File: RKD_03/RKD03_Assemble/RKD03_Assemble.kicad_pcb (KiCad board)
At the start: 2 copper layers, 97.7 x 97.6 mm, 36 parts, among them SW1 SW_Push, SW10 SW_Push, SW11 RotaryEncoder_Switch, SW12 SW_Push, SW13 SW_Push, SW14 RotaryEncoder_Switch, SW2 RotaryEncoder_Switch, SW3 SW_Push, SW4 SW_Push, SW5 RotaryEncoder_Switch, SW6 SW_Push, SW7 SW_Push, SW8 RotaryEncoder_Switch, SW9 SW_Push, U1 Pico

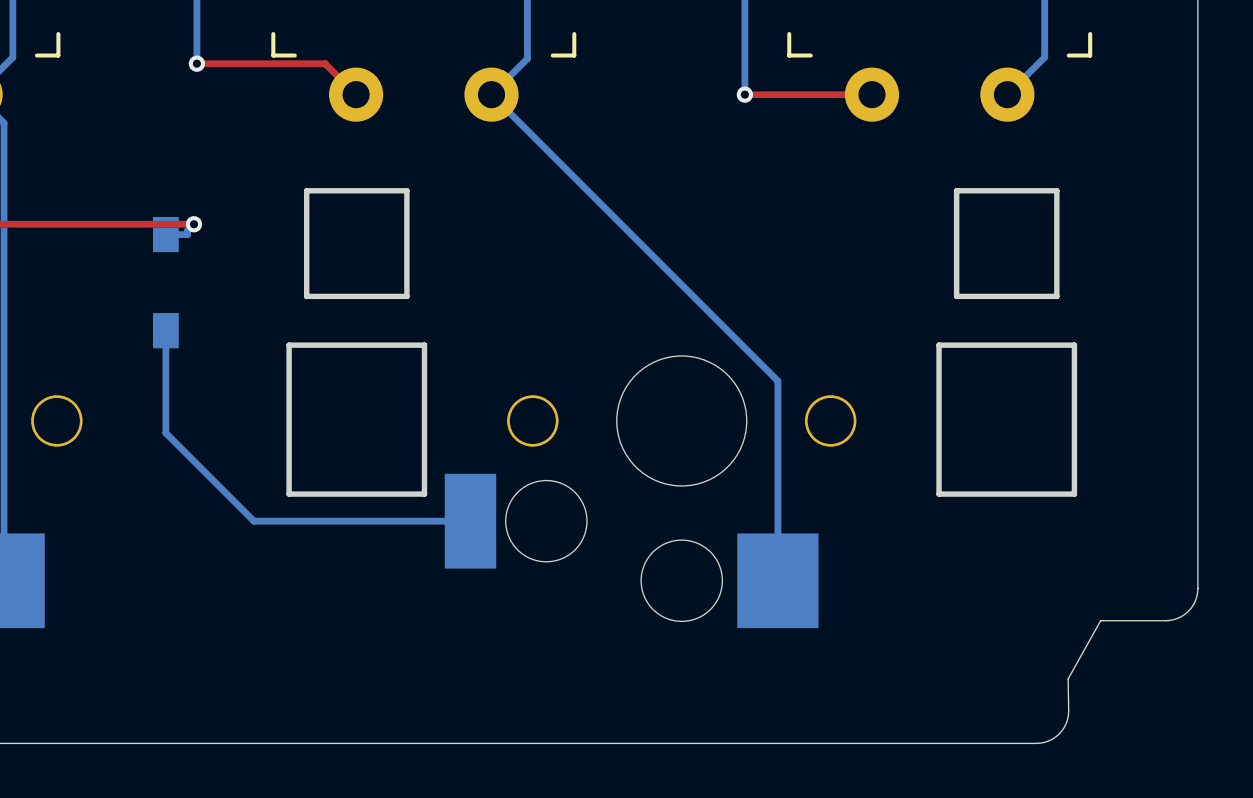
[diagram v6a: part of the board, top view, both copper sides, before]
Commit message: RKD03 新フットプリントの検証
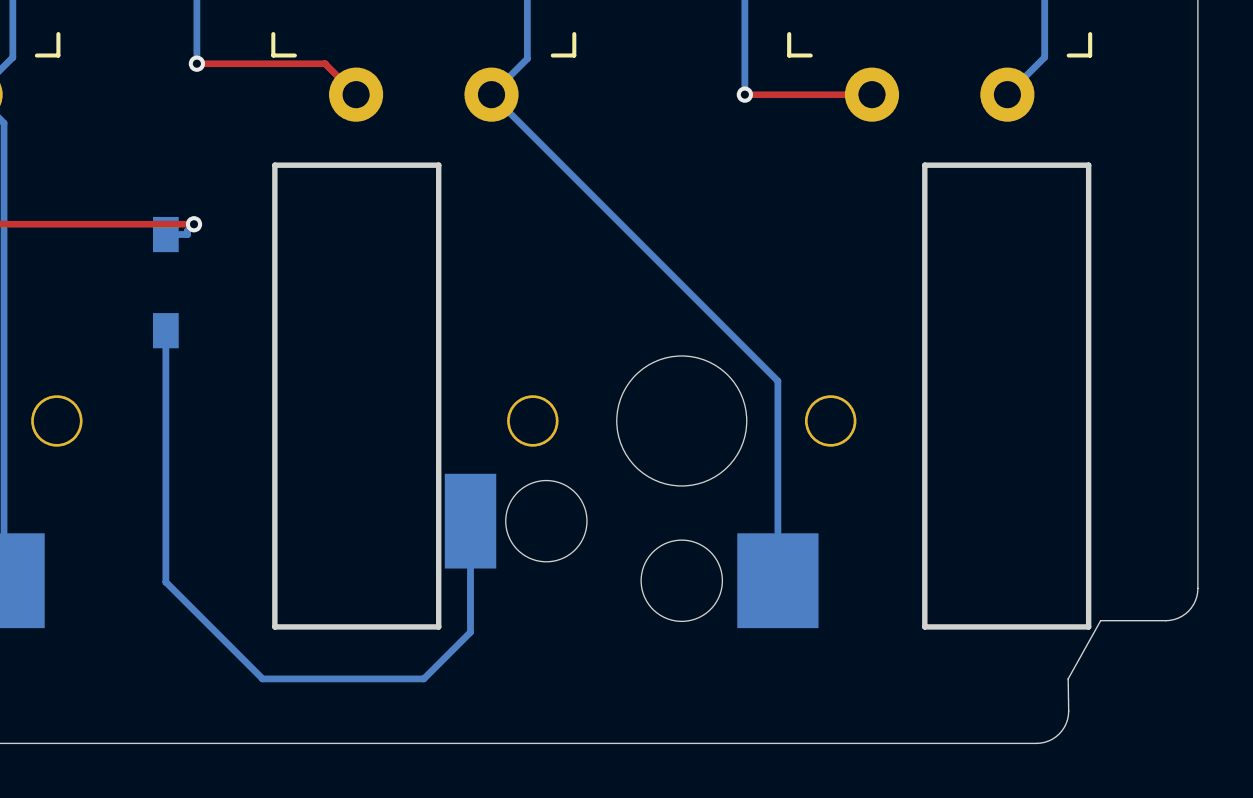
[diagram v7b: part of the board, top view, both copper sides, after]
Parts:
- SW12: footprint Rikkodo_FootPrint:rkd_Choc_v1v2_Hotswap_2u -> Rikkodo_FootPrint:rkd_Choc_v1v2_Hotswap_2u_Gat
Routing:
- net Net-(D12-A): track 16.4 -> 26.8 mm
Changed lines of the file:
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@@
 		)
 	)
-	(footprint "Rikkodo_FootPrint:rkd_Choc_v1v2_Hotswap_2u"
+	(footprint "Rikkodo_FootPrint:rkd_Choc_v1v2_Hotswap_2u_Gat"
 		(layer "F.Cu")
 		(at 121.44375 102.39375)
@@
 			)
 		)
-		(property "Footprint" "Rikkodo_FootPrint:rkd_Choc_v1v2_Hotswap_2u"
+		(property "Footprint" "Rikkodo_FootPrint:rkd_Choc_v1v2_Hotswap_2u_Gat"
 			(at 0 0 0)
 			(layer "F.Fab")
@@
 		)
 		(fp_line
-			(start -14.5 -2.8)
-			(end -9.5 -2.8)
+			(start -15.025 -9.445)
+			(end -8.975 -9.445)
 			(stroke
 				(width 0.2)
@@
 		)
 		(fp_line
-			(start -14.5 2.7)
-			(end -14.5 -2.8)
+			(start -15.025 7.605)
+			(end -15.025 -9.445)
 			(stroke
 				(width 0.2)
@@
 		)
 		(fp_line
-			(start -13.85 -8.5)
-			(end -10.15 -8.5)
+			(start -8.975 -9.445)
+			(end -8.975 7.605)
 			(stroke
 				(width 0.2)
@@
 		)
 		(fp_line
-			(start -13.85 -4.6)
-			(end -13.85 -8.5)
+			(start -8.975 7.605)
+			(end -15.025 7.605)
 			(stroke
 				(width 0.2)
@@
 		)
 		(fp_line
-			(start -10.15 -8.5)
-			(end -10.15 -4.6)
+			(start 8.975 -9.445)
+			(end 8.975 7.605)
 			(stroke
 				(width 0.2)
@@
 		)
 		(fp_line
-			(start -10.15 -4.6)
-			(end -13.85 -4.6)
+			(start 8.975 7.605)
+			(end 15.025 7.605)
 			(stroke
 				(width 0.2)
@@
 		)
 		(fp_line
-			(start -9.5 -2.8)
-			(end -9.5 2.7)
+			(start 15.025 -9.445)
+			(end 8.975 -9.445)
 			(stroke
 				(width 0.2)
@@
 		)
 		(fp_line
-			(start -9.5 2.7)
-			(end -14.5 2.7)
-			(stroke
-				(width 0.2)
-				(type solid)
-			)
-			(layer "Edge.Cuts")
-		)
-		(fp_line
-			(start 9.5 -2.8)
-			(end 9.5 2.7)
-			(stroke
-				(width 0.2)
-				(type solid)
-			)
-			(layer "Edge.Cuts")
-		)
-		(fp_line
-			(start 9.5 2.7)
-			(end 14.5 2.7)
-			(stroke
-				(width 0.2)
-				(type solid)
-			)
-			(layer "Edge.Cuts")
-		)
-		(fp_line
-			(start 10.15 -8.5)
-			(end 10.15 -4.6)
-			(stroke
-				(width 0.2)
-				(type solid)
-			)
-			(layer "Edge.Cuts")
-		)
-		(fp_line
-			(start 10.15 -4.6)
-			(end 13.85 -4.6)
-			(stroke
-				(width 0.2)
-				(type solid)
-			)
-			(layer "Edge.Cuts")
-		)
-		(fp_line
-			(start 13.85 -8.5)
-			(end 10.15 -8.5)
-			(stroke
-				(width 0.2)
-				(type solid)
-			)
-			(layer "Edge.Cuts")
-		)
-		(fp_line
-			(start 13.85 -8.5)
-			(end 13.85 -4.6)
-			(stroke
-				(width 0.2)
-				(type solid)
-			)
-			(layer "Edge.Cuts")
-		)
-		(fp_line
-			(start 14.5 -2.8)
-			(end 9.5 -2.8)
-			(stroke
-				(width 0.2)
-				(type solid)
-			)
-			(layer "Edge.Cuts")
-		)
-		(fp_line
-			(start 14.5 2.7)
-			(end 14.5 -2.8)
+			(start 15.025 7.605)
+			(end 15.025 -9.445)
 			(stroke
 				(width 0.2)
@@
 	)
 	(segment
-		(start 102.3938 102.842)
-		(end 102.3938 99.0599)
+		(start 105.965625 111.91875)
+		(end 102.3938 108.346925)
 		(width 0.25)
 		(layer "B.Cu")
@@
 	(segment
 		(start 113.64375 106.09375)
-		(end 105.64555 106.09375)
+		(end 113.64375 110.19375)
+		(width 0.25)
+		(layer "B.Cu")
+		(net 31)
+	)
+	(segment
+		(start 102.3938 108.346925)
+		(end 102.3938 99.0599)
+		(width 0.25)
+		(layer "B.Cu")
+		(net 31)
+	)
+	(segment
+		(start 111.91875 111.91875)
+		(end 105.965625 111.91875)
 		(width 0.25)
 		(layer "B.Cu")
@@
 	)
 	(segment
-		(start 105.64555 106.09375)
-		(end 102.3938 102.842)
+		(start 113.64375 110.19375)
+		(end 111.91875 111.91875)
 		(width 0.25)
 		(layer "B.Cu")

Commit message: RKD03 AddName
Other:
- board text added: "RKD03_v2.0"
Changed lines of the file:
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@@
 		(layer "Edge.Cuts")
+	)
+	(gr_text "RKD03_v2.0"
+		(at 59.53125 95.25 0)
+		(layer "B.SilkS")
+		(effects
+			(font
+				(size 1 1)
+				(thickness 0.1)
+			)
+			(justify left bottom mirror)
+		)
 	)
 	(segment
